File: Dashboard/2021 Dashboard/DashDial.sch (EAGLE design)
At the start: 31 parts, among them IC2 TLC5952DAP, J1 ESW-104-23-L-D, J2 ESW-104-23-L-D, U1 LOGIC SHIFTER, X2 SERVO

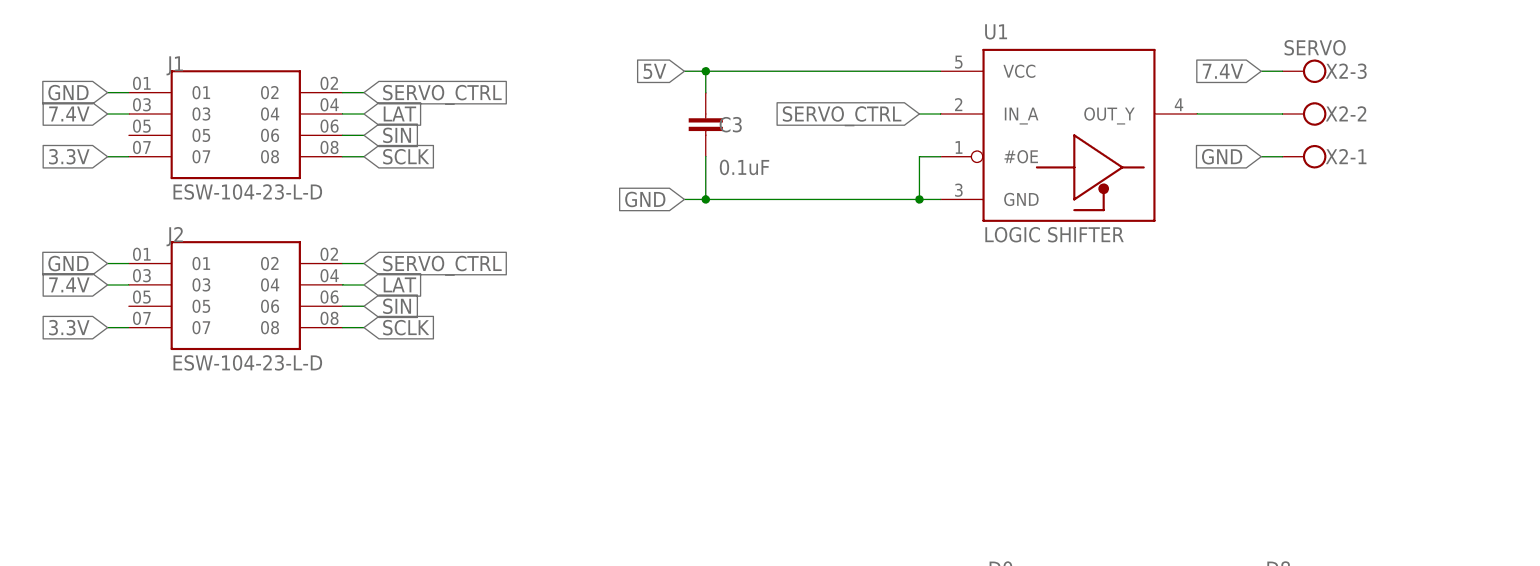
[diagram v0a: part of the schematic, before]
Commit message: Moved phat connector
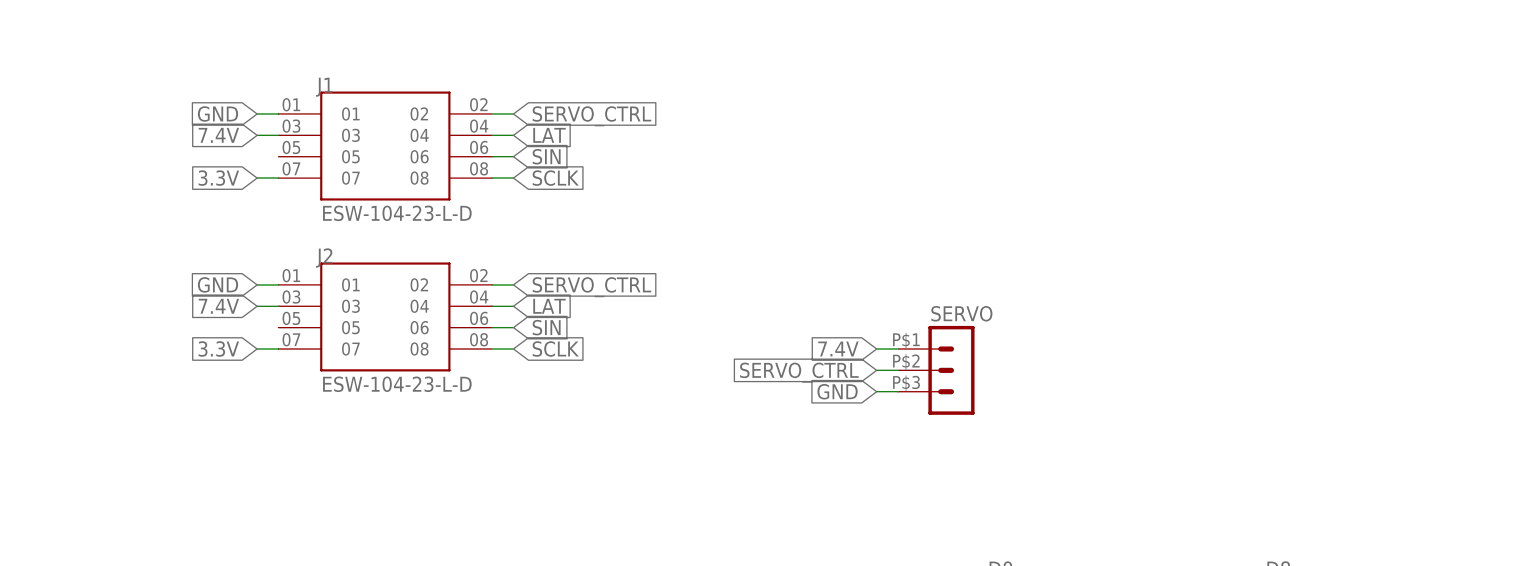
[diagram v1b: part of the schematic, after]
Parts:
- removed C3: 0.1uF, SparkFun-Capacitors:0.1UF-0603-25V-(+80/-20%)
- removed U1: LOGIC SHIFTER, MC74VHC1GT125:MC74VHC1GT125DF
- removed X2: SERVO, con-wago-500:W237-103
- added SERVO: (no value), GTOR - Microfit Connector:HEADER_POS3_43650-0315
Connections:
- removed net 5V: C3.1, U1.VCC
- removed net N$1: U1.OUT_Y, X2-2.KL
- net 7.4V: now also SERVO.1; no longer X2-3.KL
- net GND: now also SERVO.3; no longer C3.2, U1.#OE, U1.GND, X2-1.KL
- net SERVO_CTRL: now also SERVO.2; no longer U1.IN_A
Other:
- moved on the sheet: J1, J2

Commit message: More work done to dash hub and dial, gps board added
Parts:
- removed R4: 3k, SparkFun-Resistors:RESISTORAXIAL-0.3
- added R1: (no value), GTOR - Passive Components:RES_SMDR0603
- added SERVO1: (no value), GTOR - Microfit Connector:HEADER_POS3_43650-0315
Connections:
- net 7.4V: now also SERVO1.1
- net GND: now also R1.2, SERVO1.3; no longer R4.1
- net N$31: now also R1.1; no longer R4.2
- net SERVO_CTRL: now also SERVO1.2
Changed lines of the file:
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@@
 <part name="J2" library="ESW-104-23-L-D" deviceset="ESW-104-23-L-D" device=""/>
 <part name="IC2" library="GTOR - Active Components" deviceset="TLC5952DAP" device=""/>
-<part name="R4" library="SparkFun-Resistors" deviceset="RESISTOR" device="AXIAL-0.3" value="3k"/>
 <part name="+3V5" library="GTOR - Documation Frame" deviceset="+3V3" device=""/>
 <part name="SERVO" library="GTOR - Microfit Connector" deviceset="HEADER_POS3_?" device="43650-0315"/>
+<part name="R1" library="GTOR - Passive Components" deviceset="RES_SMD" device="R0603" package3d_urn="urn:adsk.eagle:package:23555/3"/>
+<part name="SERVO1" library="GTOR - Microfit Connector" deviceset="HEADER_POS3_?" device="43650-0315"/>
 </parts>
 <sheets>
@@
 <text x="-22.86" y="152.4" size="5.08" layer="98">Inputs</text>
 <wire x1="17.78" y1="132.08" x2="17.78" y2="104.14" width="0.1524" layer="98"/>
-<wire x1="17.78" y1="104.14" x2="68.58" y2="104.14" width="0.1524" layer="98"/>
-<wire x1="68.58" y1="104.14" x2="68.58" y2="132.08" width="0.1524" layer="98"/>
-<wire x1="68.58" y1="132.08" x2="17.78" y2="132.08" width="0.1524" layer="98"/>
+<wire x1="17.78" y1="104.14" x2="88.9" y2="104.14" width="0.1524" layer="98"/>
+<wire x1="88.9" y1="104.14" x2="88.9" y2="132.08" width="0.1524" layer="98"/>
+<wire x1="88.9" y1="132.08" x2="17.78" y2="132.08" width="0.1524" layer="98"/>
 <text x="22.86" y="124.46" size="5.08" layer="98">Servo Control</text>
 <wire x1="-45.72" y1="101.6" x2="-45.72" y2="20.32" width="0.1524" layer="98"/>
@@
 <attribute name="VALUE" x="-3.81" y="78.74" size="1.778" layer="96" align="center-left"/>
 </instance>
-<instance part="R4" gate="G$1" x="17.78" y="38.1" smashed="yes" rot="R180">
-<attribute name="NAME" x="17.78" y="36.576" size="1.778" layer="95" font="vector" rot="R180" align="bottom-center"/>
-<attribute name="VALUE" x="17.78" y="39.624" size="1.778" layer="96" font="vector" rot="R180" align="top-center"/>
-</instance>
 <instance part="+3V5" gate="G$1" x="5.08" y="43.18" smashed="yes">
 <attribute name="VALUE" x="2.54" y="38.1" size="1.778" layer="96" rot="R90"/>
@@
 <attribute name="VALUE" x="44.45" y="104.14" size="1.778" layer="96"/>
 <attribute name="NAME" x="44.45" y="117.602" size="1.778" layer="95"/>
+</instance>
+<instance part="R1" gate="G$1" x="17.78" y="38.1" smashed="yes">
+<attribute name="NAME" x="13.97" y="39.5986" size="1.778" layer="95"/>
+<attribute name="VALUE" x="13.97" y="34.798" size="1.778" layer="96"/>
+</instance>
+<instance part="SERVO1" gate="G$1" x="78.74" y="111.76" smashed="yes">
+<attribute name="VALUE" x="77.47" y="104.14" size="1.778" layer="96"/>
+<attribute name="NAME" x="77.47" y="117.602" size="1.778" layer="95"/>
 </instance>
 </instances>
@@
 </segment>
 <segment>
-<pinref part="R4" gate="G$1" pin="1"/>
 <wire x1="22.86" y1="38.1" x2="25.4" y2="38.1" width="0.1524" layer="91"/>
 <label x="25.4" y="38.1" size="1.778" layer="95" xref="yes"/>
+<pinref part="R1" gate="G$1" pin="2"/>
 </segment>
 <segment>
@@
 <pinref part="SERVO" gate="G$1" pin="3"/>
 </segment>
+<segment>
+<wire x1="73.66" y1="109.22" x2="71.12" y2="109.22" width="0.1524" layer="91"/>
+<label x="71.12" y="109.22" size="1.778" layer="95" rot="R180" xref="yes"/>
+<pinref part="SERVO1" gate="G$1" pin="3"/>
+</segment>
 </net>
 <net name="7.4V" class="0">
@@
 <pinref part="SERVO" gate="G$1" pin="1"/>
 </segment>
+<segment>
+<wire x1="73.66" y1="114.3" x2="71.12" y2="114.3" width="0.1524" layer="91"/>
+<label x="71.12" y="114.3" size="1.778" layer="95" rot="R180" xref="yes"/>
+<pinref part="SERVO1" gate="G$1" pin="1"/>
+</segment>
 </net>
 <net name="SIN" class="0">
@@
 <pinref part="SERVO" gate="G$1" pin="2"/>
 </segment>
+<segment>
+<wire x1="73.66" y1="111.76" x2="71.12" y2="111.76" width="0.1524" layer="91"/>
+<label x="71.12" y="111.76" size="1.778" layer="95" rot="R180" xref="yes"/>
+<pinref part="SERVO1" gate="G$1" pin="2"/>
+</segment>
 </net>
 <net name="+3V3" class="0">
@@
 <net name="N$31" class="0">
 <segment>
-<pinref part="R4" gate="G$1" pin="2"/>
 <wire x1="0" y1="38.1" x2="12.7" y2="38.1" width="0.1524" layer="91"/>
 <pinref part="IC2" gate="G$1" pin="IREF"/>
+<pinref part="R1" gate="G$1" pin="1"/>
 </segment>
 </net>
@@
 which will not be processed correctly with this version.
 </note>
+<note version="8.3" severity="warning">
+Since Version 8.3, EAGLE supports URNs for individual library
+assets (packages, symbols, and devices). The URNs of those assets
+will not be understood (or retained) with this version.
+</note>
+<note version="8.3" severity="warning">
+Since Version 8.3, EAGLE supports the association of 3D packages
+with devices in libraries, schematics, and board files. Those 3D
+packages will not be understood (or retained) with this version.
+</note>
+<note version="8.4" severity="warning">
+Since Version 8.4, EAGLE supports properties for SPICE simulation.
+Probes in schematics and SPICE mapping objects found in parts and library devices
+will not be understood with this version. Update EAGLE to the latest version
+for full support of SPICE simulation.
+</note>
 </compatibility>

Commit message: Fixed the dashhub #everything
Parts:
- SERVO, SERVO1: device GTOR - Microfit Connector:HEADER_POS3_43650-0315 -> GTOR - Microfit Connector:HEADER_POS3_43650-0300
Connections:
- removed net +3V3: IC2.VCC
- removed net N$30: IC2.GND
- net 3.3V: now also IC2.VCC
- net GND: now also IC2.GND
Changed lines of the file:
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@@
 <part name="J2" library="ESW-104-23-L-D" deviceset="ESW-104-23-L-D" device=""/>
 <part name="IC2" library="GTOR - Active Components" deviceset="TLC5952DAP" device=""/>
-<part name="+3V5" library="GTOR - Documation Frame" deviceset="+3V3" device=""/>
-<part name="SERVO" library="GTOR - Microfit Connector" deviceset="HEADER_POS3_?" device="43650-0315"/>
+<part name="SERVO" library="GTOR - Microfit Connector" deviceset="HEADER_POS3_?" device="43650-0300"/>
 <part name="R1" library="GTOR - Passive Components" deviceset="RES_SMD" device="R0603" package3d_urn="urn:adsk.eagle:package:23555/3"/>
-<part name="SERVO1" library="GTOR - Microfit Connector" deviceset="HEADER_POS3_?" device="43650-0315"/>
+<part name="SERVO1" library="GTOR - Microfit Connector" deviceset="HEADER_POS3_?" device="43650-0300"/>
 </parts>
 <sheets>
@@
 <attribute name="VALUE" x="-3.81" y="78.74" size="1.778" layer="96" align="center-left"/>
 </instance>
-<instance part="+3V5" gate="G$1" x="5.08" y="43.18" smashed="yes">
-<attribute name="VALUE" x="2.54" y="38.1" size="1.778" layer="96" rot="R90"/>
-</instance>
 <instance part="SERVO" gate="G$1" x="45.72" y="111.76" smashed="yes">
 <attribute name="VALUE" x="44.45" y="104.14" size="1.778" layer="96"/>
@@
 <label x="-35.56" y="114.3" size="1.778" layer="95" rot="R180" xref="yes"/>
 </segment>
+<segment>
+<wire x1="0" y1="40.64" x2="5.08" y2="40.64" width="0.1524" layer="91"/>
+<pinref part="IC2" gate="G$1" pin="VCC"/>
+<label x="5.08" y="40.64" size="1.778" layer="95" xref="yes"/>
+</segment>
 </net>
 <net name="GND" class="0">
@@
 </segment>
 <segment>
-<label x="-33.02" y="73.66" size="1.778" layer="95" rot="R180" xref="yes"/>
-<label x="-33.02" y="73.66" size="1.778" layer="95" rot="R180" xref="yes"/>
-</segment>
-<segment>
 <wire x1="22.86" y1="38.1" x2="25.4" y2="38.1" width="0.1524" layer="91"/>
 <label x="25.4" y="38.1" size="1.778" layer="95" xref="yes"/>
@@
 <pinref part="SERVO1" gate="G$1" pin="3"/>
 </segment>
+<segment>
+<pinref part="IC2" gate="G$1" pin="GND"/>
+<wire x1="-30.48" y1="73.66" x2="-33.02" y2="73.66" width="0.1524" layer="91"/>
+<label x="-33.02" y="73.66" size="1.778" layer="95" rot="R180" xref="yes"/>
+</segment>
 </net>
 <net name="7.4V" class="0">
@@
 <pinref part="IC2" gate="G$1" pin="OUTR0"/>
 <wire x1="-33.02" y1="63.5" x2="-30.48" y2="63.5" width="0.1524" layer="91"/>
+<label x="-33.02" y="63.5" size="1.778" layer="95" rot="R180" xref="yes"/>
 </segment>
 </net>
@@
 <pinref part="IC2" gate="G$1" pin="OUTG0"/>
 <wire x1="-30.48" y1="60.96" x2="-33.02" y2="60.96" width="0.1524" layer="91"/>
+<label x="-33.02" y="60.96" size="1.778" layer="95" rot="R180" xref="yes"/>
 </segment>
 </net>
@@
 <pinref part="IC2" gate="G$1" pin="OUTB0"/>
 <wire x1="-30.48" y1="58.42" x2="-33.02" y2="58.42" width="0.1524" layer="91"/>
+<label x="-33.02" y="58.42" size="1.778" layer="95" rot="R180" xref="yes"/>
 </segment>
 </net>
@@
 <pinref part="IC2" gate="G$1" pin="OUTR1"/>
 <wire x1="-33.02" y1="55.88" x2="-30.48" y2="55.88" width="0.1524" layer="91"/>
+<label x="-33.02" y="55.88" size="1.778" layer="95" rot="R180" xref="yes"/>
 </segment>
 </net>
@@
 <pinref part="IC2" gate="G$1" pin="OUTG1"/>
 <wire x1="-33.02" y1="53.34" x2="-30.48" y2="53.34" width="0.1524" layer="91"/>
+<label x="-33.02" y="53.34" size="1.778" layer="95" rot="R180" xref="yes"/>
 </segment>
 </net>
@@
 <pinref part="IC2" gate="G$1" pin="OUTB1"/>
 <wire x1="-30.48" y1="50.8" x2="-33.02" y2="50.8" width="0.1524" layer="91"/>
+<label x="-33.02" y="50.8" size="1.778" layer="95" rot="R180" xref="yes"/>
 </segment>
 </net>
@@
 <pinref part="IC2" gate="G$1" pin="OUTR2"/>
 <wire x1="-33.02" y1="48.26" x2="-30.48" y2="48.26" width="0.1524" layer="91"/>
+<label x="-33.02" y="48.26" size="1.778" layer="95" rot="R180" xref="yes"/>
 </segment>
 </net>
@@
 <pinref part="IC2" gate="G$1" pin="OUTG2"/>
 <wire x1="-33.02" y1="45.72" x2="-30.48" y2="45.72" width="0.1524" layer="91"/>
+<label x="-33.02" y="45.72" size="1.778" layer="95" rot="R180" xref="yes"/>
 </segment>
 </net>
@@
 <pinref part="IC2" gate="G$1" pin="OUTB2"/>
 <wire x1="-33.02" y1="43.18" x2="-30.48" y2="43.18" width="0.1524" layer="91"/>
+<label x="-33.02" y="43.18" size="1.778" layer="95" rot="R180" xref="yes"/>
 </segment>
 </net>
@@
 <pinref part="IC2" gate="G$1" pin="OUTR3"/>
 <wire x1="-30.48" y1="40.64" x2="-33.02" y2="40.64" width="0.1524" layer="91"/>
+<label x="-33.02" y="40.64" size="1.778" layer="95" rot="R180" xref="yes"/>
 </segment>
 </net>
@@
 <pinref part="IC2" gate="G$1" pin="OUTG3"/>
 <wire x1="-33.02" y1="38.1" x2="-30.48" y2="38.1" width="0.1524" layer="91"/>
+<label x="-33.02" y="38.1" size="1.778" layer="95" rot="R180" xref="yes"/>
 </segment>
 </net>
@@
 <pinref part="IC2" gate="G$1" pin="OUTB3"/>
 <wire x1="-33.02" y1="35.56" x2="-30.48" y2="35.56" width="0.1524" layer="91"/>
+<label x="-33.02" y="35.56" size="1.778" layer="95" rot="R180" xref="yes"/>
 </segment>
 </net>
@@
 <pinref part="IC2" gate="G$1" pin="OUTR4"/>
 <wire x1="-33.02" y1="33.02" x2="-30.48" y2="33.02" width="0.1524" layer="91"/>
+<label x="-33.02" y="33.02" size="1.778" layer="95" rot="R180" xref="yes"/>
 </segment>
 </net>
@@
 <pinref part="IC2" gate="G$1" pin="OUTG4"/>
 <wire x1="2.54" y1="73.66" x2="0" y2="73.66" width="0.1524" layer="91"/>
+<label x="2.54" y="73.66" size="1.778" layer="95" xref="yes"/>
 </segment>
 </net>
@@
 <pinref part="IC2" gate="G$1" pin="OUTB4"/>
 <wire x1="0" y1="71.12" x2="2.54" y2="71.12" width="0.1524" layer="91"/>
+<label x="2.54" y="71.12" size="1.778" layer="95" xref="yes"/>
 </segment>
 </net>
@@
 <pinref part="IC2" gate="G$1" pin="OUTR5"/>
 <wire x1="2.54" y1="68.58" x2="0" y2="68.58" width="0.1524" layer="91"/>
+<label x="2.54" y="68.58" size="1.778" layer="95" xref="yes"/>
 </segment>
 </net>
@@
 <pinref part="IC2" gate="G$1" pin="OUTG5"/>
 <wire x1="2.54" y1="66.04" x2="0" y2="66.04" width="0.1524" layer="91"/>
+<label x="2.54" y="66.04" size="1.778" layer="95" xref="yes"/>
 </segment>
 </net>
@@
 <pinref part="IC2" gate="G$1" pin="OUTB5"/>
 <wire x1="2.54" y1="63.5" x2="0" y2="63.5" width="0.1524" layer="91"/>
+<label x="2.54" y="63.5" size="1.778" layer="95" xref="yes"/>
 </segment>
 </net>
@@
 <pinref part="IC2" gate="G$1" pin="OUTR6"/>
 <wire x1="0" y1="60.96" x2="2.54" y2="60.96" width="0.1524" layer="91"/>
+<label x="2.54" y="60.96" size="1.778" layer="95" xref="yes"/>
 </segment>
 </net>
@@
 <pinref part="IC2" gate="G$1" pin="OUTG6"/>
 <wire x1="2.54" y1="58.42" x2="0" y2="58.42" width="0.1524" layer="91"/>
+<label x="2.54" y="58.42" size="1.778" layer="95" xref="yes"/>
 </segment>
 </net>
@@
 <pinref part="IC2" gate="G$1" pin="OUTB6"/>
 <wire x1="2.54" y1="55.88" x2="0" y2="55.88" width="0.1524" layer="91"/>
+<label x="2.54" y="55.88" size="1.778" layer="95" xref="yes"/>
 </segment>
 </net>
@@
 <pinref part="IC2" gate="G$1" pin="OUTR7"/>
 <wire x1="0" y1="53.34" x2="2.54" y2="53.34" width="0.1524" layer="91"/>
+<label x="2.54" y="53.34" size="1.778" layer="95" xref="yes"/>
 </segment>
 </net>
@@
 <pinref part="IC2" gate="G$1" pin="OUTG7"/>
 <wire x1="2.54" y1="50.8" x2="0" y2="50.8" width="0.1524" layer="91"/>
+<label x="2.54" y="50.8" size="1.778" layer="95" xref="yes"/>
 </segment>
 </net>
@@
 <pinref part="IC2" gate="G$1" pin="OUTB7"/>
 <wire x1="2.54" y1="48.26" x2="0" y2="48.26" width="0.1524" layer="91"/>
+<label x="2.54" y="48.26" size="1.778" layer="95" xref="yes"/>
 </segment>
 </net>
@@
 </segment>
 </net>
-<net name="+3V3" class="0">
-<segment>
-<wire x1="0" y1="40.64" x2="5.08" y2="40.64" width="0.1524" layer="91"/>
-<pinref part="IC2" gate="G$1" pin="VCC"/>
-<pinref part="+3V5" gate="G$1" pin="+3V3"/>
-</segment>
-</net>
-<net name="N$30" class="0">
-<segment>
-<wire x1="-30.48" y1="73.66" x2="-33.02" y2="73.66" width="0.1524" layer="91"/>
-<pinref part="IC2" gate="G$1" pin="GND"/>
-</segment>
-</net>

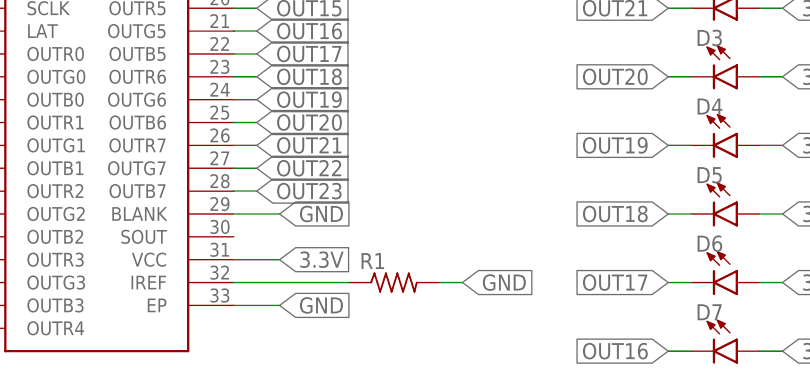
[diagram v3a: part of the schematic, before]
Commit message: Added resistor values to dashhub and board
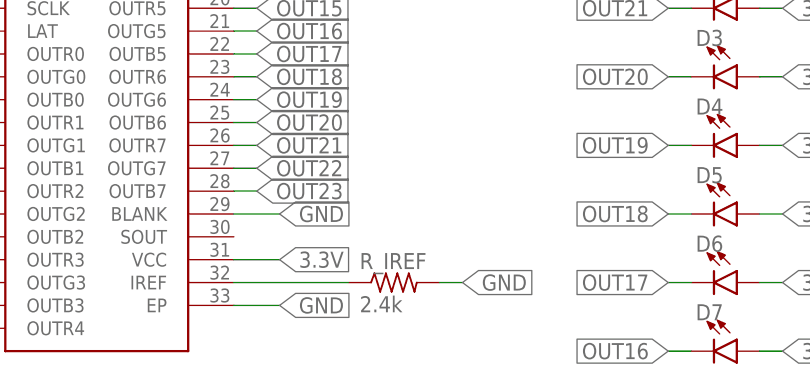
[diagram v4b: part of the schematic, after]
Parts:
- R_IREF: value (none) -> 2.4k
- renumbered R1 to R_IREF
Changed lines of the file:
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@@
 <part name="IC2" library="GTOR - Active Components" deviceset="TLC5952DAP" device=""/>
 <part name="SERVO" library="GTOR - Microfit Connector" deviceset="HEADER_POS3_?" device="43650-0300"/>
-<part name="R1" library="GTOR - Passive Components" deviceset="RES_SMD" device="R0603" package3d_urn="urn:adsk.eagle:package:23555/3"/>
+<part name="R_IREF" library="GTOR - Passive Components" deviceset="RES_SMD" device="R0603" package3d_urn="urn:adsk.eagle:package:23555/3" value="2.4k"/>
 <part name="SERVO1" library="GTOR - Microfit Connector" deviceset="HEADER_POS3_?" device="43650-0300"/>
 </parts>
@@
 <attribute name="NAME" x="44.45" y="117.602" size="1.778" layer="95"/>
 </instance>
-<instance part="R1" gate="G$1" x="17.78" y="38.1" smashed="yes">
+<instance part="R_IREF" gate="G$1" x="17.78" y="38.1" smashed="yes">
 <attribute name="NAME" x="13.97" y="39.5986" size="1.778" layer="95"/>
 <attribute name="VALUE" x="13.97" y="34.798" size="1.778" layer="96"/>
@@
 <wire x1="22.86" y1="38.1" x2="25.4" y2="38.1" width="0.1524" layer="91"/>
 <label x="25.4" y="38.1" size="1.778" layer="95" xref="yes"/>
-<pinref part="R1" gate="G$1" pin="2"/>
+<pinref part="R_IREF" gate="G$1" pin="2"/>
 </segment>
 <segment>
@@
 <wire x1="0" y1="38.1" x2="12.7" y2="38.1" width="0.1524" layer="91"/>
 <pinref part="IC2" gate="G$1" pin="IREF"/>
-<pinref part="R1" gate="G$1" pin="1"/>
-</segment>
-</net>
+<pinref part="R_IREF" gate="G$1" pin="1"/>
+</segment>
+</net>
